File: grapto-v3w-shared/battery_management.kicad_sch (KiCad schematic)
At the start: 18 parts, among them U8 AP9211S-AL, U9 MCP7383x-2xMC

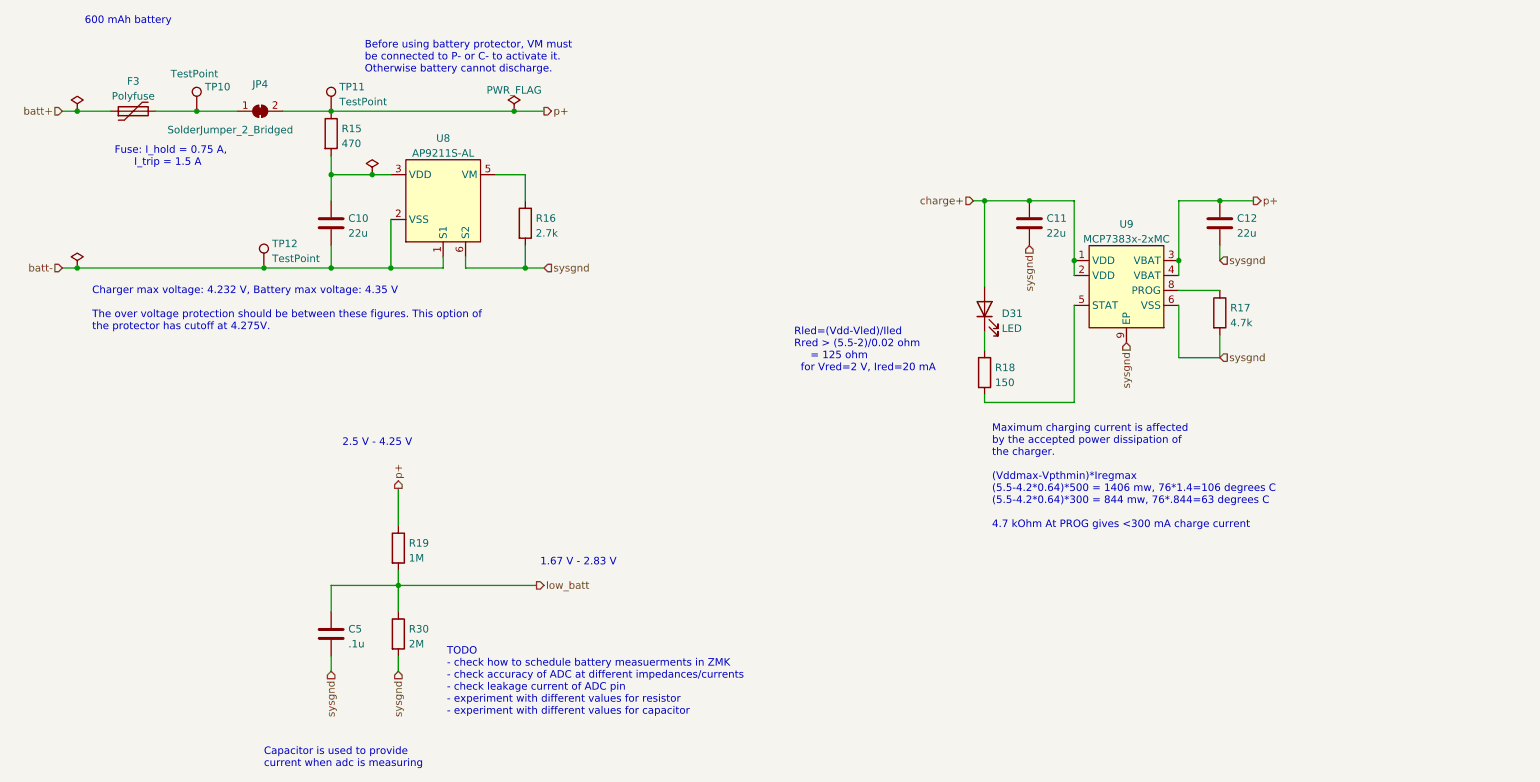
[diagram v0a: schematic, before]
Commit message: Redesign pcb with new mcu and charger
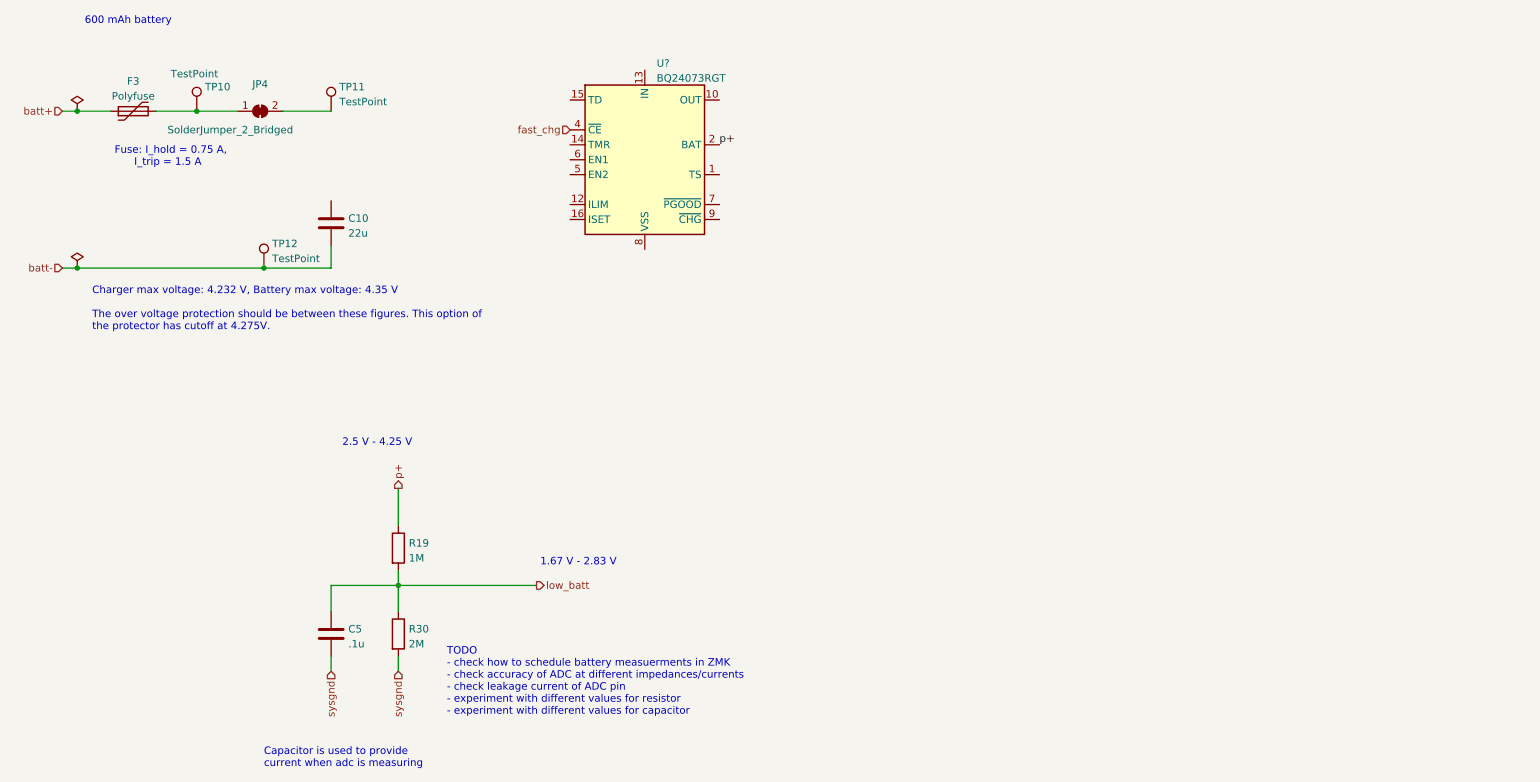
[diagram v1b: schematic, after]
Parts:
- removed C11, C12: 22u, Fuse:Fuse_0603_1608Metric_Pad1.05x0.95mm_HandSolder, symbol Device:C
- removed D31: LED, LED_SMD:LED_0805_2012Metric_Pad1.15x1.40mm_HandSolder, symbol Device:LED
- removed R15: 470, Resistor_SMD:R_0603_1608Metric_Pad0.98x0.95mm_HandSolder, symbol Device:R
- removed R16: 2.7k, Resistor_SMD:R_0603_1608Metric_Pad0.98x0.95mm_HandSolder, symbol Device:R
- removed R17: 4.7k, Resistor_SMD:R_0603_1608Metric_Pad0.98x0.95mm_HandSolder, symbol Device:R
- removed R18: 150, Resistor_SMD:R_0603_1608Metric_Pad0.98x0.95mm_HandSolder, symbol Device:R
- removed U8: AP9211S-AL, grapto-v3w:U-DFN2030-6_type_c, symbol grapto-v3w:AP9211S-AL
- removed U9: MCP7383x-2xMC, Package_DFN_QFN:DFN-8-1EP_3x2mm_P0.5mm_EP1.75x1.45mm, symbol grapto-v3w:MCP7383x-2xMC
- added U?: BQ24073RGT, Package_DFN_QFN:VQFN-16-1EP_3x3mm_P0.5mm_EP1.6x1.6mm, symbol Battery_Management:BQ24073RGT
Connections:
- net p+: now also U?.2 (BAT), U?.3 (BAT); no longer JP4.2 (B), TP11.1
- new net: JP4.2 (B), TP11.1
- new net: U?.10 (OUT), U?.11 (OUT)
- new net: U?.17 (VSS), U?.8 (VSS)
- new net fast_chg: U?.4 (~{CE})
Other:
- note removed: "Before using battery protector, VM must be connected to P- or C- to activate it. Otherwise battery cannot discharge."
- note removed: "Maximum charging current is affected by the accepted power dissipation of the charger. (Vddmax-Vpthmin)*Iregmax (5.5-4.2*0.64)*500 = 1406 mw, 76*1.4=106 degrees C (5.5-4.2*0.64)*300 = 844 mw, 76*.844=63 degrees C 4.7 kOhm At PROG gives <300 mA charge current"
- note removed: "Rled=(Vdd-Vled)/Iled Rred > (5.5-2)/0.02 ohm = 125 ohm for Vred=2 V, Ired=20 mA"

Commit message: schematic rewrite draft done.
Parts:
- removed TP12: TestPoint, grapto-v3w:TestPoint_THTPad_D2.0mm_Drill1.0mm, symbol Connector:TestPoint
- added C1: 1u, Fuse:Fuse_0603_1608Metric_Pad1.05x0.95mm_HandSolder, symbol Device:C
- added D31, D32, D33: LED, LED_SMD:LED_0805_2012Metric_Pad1.15x1.40mm_HandSolder, symbol Device:LED
- added R2, R3, R5: 60, Resistor_SMD:R_0603_1608Metric_Pad0.98x0.95mm_HandSolder, symbol Device:R
- added R4: 10K, Resistor_SMD:R_0603_1608Metric_Pad0.98x0.95mm_HandSolder, symbol Device:R
- added R6: 5.6, Resistor_SMD:R_0603_1608Metric_Pad0.98x0.95mm_HandSolder, symbol Device:R
- added R7: 3.3K, Resistor_SMD:R_0603_1608Metric_Pad0.98x0.95mm_HandSolder, symbol Device:R
- added R8: 2.2K, Resistor_SMD:R_0603_1608Metric_Pad0.98x0.95mm_HandSolder, symbol Device:R
- gave numbers to parts that had none: 1
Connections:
- net batt- is gone; now on net sysgnd: C10.2
- net p+ is gone; now on net bat_fused: R19.1, U2.2 (BAT), U2.3 (BAT)
- net fast_chg: now also U2.5 (EN2), R6.1; no longer U2.4 (~{CE})
- net sysgnd: now also U2.15 (TD), U2.17 (VSS), U2.4 (~{CE}), U2.6 (EN1), U2.8 (VSS), C1.2, D33.1 (K), R4.2, R7.2, R8.2
- net bat_fused: now reaches JP4.2 (B), TP11.1
- net bat_fused: now also C10.1
- net at U2.1 (TS): now also R4.1
- net vsys: now reaches U2.10 (OUT), U2.11 (OUT)
- net vsys: now also R2.1, R3.1
- net at U2.12 (ILIM): now also R7.1
- net vusb: now reaches U2.13 (IN)
- net vusb: now also C1.1
- net at U2.16 (ISET): now also R8.1
- net at U2.7 (~{PGOOD}): now also D32.1 (K)
- net at U2.9 (~{CHG}): now also D31.1 (K)
- net batt+ renamed bat+
- net low_batt renamed bat_level
- new net: R2.2, R5.1
- new net: D32.2 (A), R5.2
- new net: D31.2 (A), R3.2
- new net: D33.2 (A), R6.2
- no-connect marks 0 -> 1
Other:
- note added: "2 V - 2.93 V"
- note added: "3 V - 4.4 V"
- note added: "Blue"
- note added: "Green"
- note added: "IN cap needs to be smaller than 10 uF to prevent too large USB inrush currents"
- note added: "I_led = 20 mA V_led = 3.25 V R_led = (V - V_led)/I_led R_green = (4.4 - 3.2)/0.02 = 60 ohm R_blue = (3.3 - 3.2)/0.02 = 5 ohm R_red = (4.4 - 2)/0.02 = 120 ohm"
- note added: "RILIM = KILIM/ILIM ~ 1525/0.5 = 3.05 kOhm, Use 3.3 kOhm RISET = KISET/ISET ~ 890/0.4 Ohm = 2.225 KOhm, use 2.2 kOhm ITERM leave unconnected for default termination current TD Connect to ground to enable charger termination TMR leave unconnected for default timer values TS Connect with 10 KOhm resistor to ground (enable charging without batt temp sensor) EN1 connect to logic low to use USB current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"
- note added: "Red"
- note removed: "1.67 V - 2.83 V"
- note removed: "2.5 V - 4.25 V"
- note removed: "Charger max voltage: 4.232 V, Battery max voltage: 4.35 V The over voltage protection should be between these figures. This option of the protector has cutoff at 4.275V."
- moved on the sheet: C10, C5, F3, JP4, R19, R30, TP10, TP11, U2

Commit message: Schematic work.
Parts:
- removed D32: LED, LED_SMD:LED_0805_2012Metric_Pad1.15x1.40mm_HandSolder, symbol Device:LED
- removed R2, R5: 60, Resistor_SMD:R_0603_1608Metric_Pad0.98x0.95mm_HandSolder, symbol Device:R
- removed U2: BQ24073RGT, Package_DFN_QFN:VQFN-16-1EP_3x3mm_P0.5mm_EP1.6x1.6mm, symbol Battery_Management:BQ24073RGT
- added SW?: power slider, symbol Switch:SW_Push_SPDT
- added U?: BQ24075RGT, Package_DFN_QFN:VQFN-16-1EP_3x3mm_P0.5mm_EP1.6x1.6mm, symbol Battery_Management:BQ24075RGT
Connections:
- net bat_fused: now also U?.2 (BAT), U?.3 (BAT)
- net fast_chg: now also U?.5 (EN2)
- net sysgnd: now also SW?.3 (C), U?.17 (VSS), U?.4 (~{CE}), U?.6 (EN1), U?.8 (VSS)
- net vsys: now also U?.10 (OUT), U?.11 (OUT)
- net vusb: now also U?.13 (IN)
- net at R4.1: now also U?.1 (TS)
- net at R8.1: now also U?.16 (ISET)
- net at D31.1 (K): now also U?.9 (~{CHG})
- net at R7.1: now also U?.12 (ILIM)
- new net: SW?.2 (B), U?.15 (SYSOFF)
- no-connect marks 1 -> 3
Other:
- note added: "SYSOFF internally pulled up to bat by high resistor. drive low to disconnect battery"
- note added: "TODO add suicide circuit triggered by mcu to save discharge battery more slowly after cutoff"

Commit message: Schematic fine-tuning.
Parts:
- removed JP4: SolderJumper_2_Bridged, Jumper:SolderJumper-2_P1.3mm_Bridged_RoundedPad1.0x1.5mm, symbol Jumper:SolderJumper_2_Bridged
- added R?: 0.01m, symbol Device:R
- added TP?: TestPoint, grapto-v3w:TestPoint_THTPad_D2.0mm_Drill1.0mm, symbol Connector:TestPoint
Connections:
- net bat_fused: now also R?.2
- net sysgnd: now also SW?.1 (A); no longer SW?.3 (C)
- net at U?.7 (~{PGOOD}): now also TP?.1
- net at F3.2, TP10.1: now also R?.1
- no-connect marks 3 -> 2
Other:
- note added: "~CE internally pulled down by 285kOhm resistor"
- moved on the sheet: R4, SW?
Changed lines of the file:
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@@
 (kicad_sch (version 20211123) (generator eeschema)
   (paper "A4")
-  (junction (at 168.91 69.85) (diameter 0) (color 0 0 0 0)
+  (junction (at 168.91 74.93) (diameter 0) (color 0 0 0 0)
   )
   (junction (at 187.325 49.53) (diameter 0) (color 0 0 0 0)
@@
   (junction (at 69.215 118.745) (diameter 0) (color 0 0 0 0)
   )
-  (no_connect (at 150.495 69.85))
+  (no_connect (at 146.05 62.23))
   (no_connect (at 174.625 72.39))
-  (no_connect (at 200.025 82.55))
-  (wire (pts (xy 168.91 74.93) (xy 168.91 69.85))
-    (stroke (width 0) (type default) (color 0 0 0 0))
-  )
   (wire (pts (xy 172.72 105.41) (xy 187.325 105.41))
     (stroke (width 0) (type default) (color 0 0 0 0))
@@
     (stroke (width 0) (type default) (color 0 0 0 0))
   )
+  (wire (pts (xy 168.91 69.85) (xy 168.91 74.93))
+    (stroke (width 0) (type default) (color 0 0 0 0))
+  )
+  (wire (pts (xy 168.91 74.93) (xy 161.925 74.93))
+    (stroke (width 0) (type default) (color 0 0 0 0))
+  )
   (wire (pts (xy 154.305 77.47) (xy 174.625 77.47))
     (stroke (width 0) (type default) (color 0 0 0 0))
@@
     (stroke (width 0) (type default) (color 0 0 0 0))
   )
-  (wire (pts (xy 205.74 73.66) (xy 211.455 73.66))
+  (wire (pts (xy 211.455 73.66) (xy 217.17 73.66))
     (stroke (width 0) (type default) (color 0 0 0 0))
   )
@@
     (stroke (width 0) (type default) (color 0 0 0 0))
   )
-  (wire (pts (xy 205.74 77.47) (xy 205.74 73.66))
+  (wire (pts (xy 211.455 77.47) (xy 211.455 73.66))
     (stroke (width 0) (type default) (color 0 0 0 0))
   )
@@
     (stroke (width 0) (type default) (color 0 0 0 0))
   )
-  (wire (pts (xy 145.415 69.85) (xy 145.415 73.025))
-    (stroke (width 0) (type default) (color 0 0 0 0))
-  )
   (wire (pts (xy 172.72 96.52) (xy 172.72 105.41))
     (stroke (width 0) (type default) (color 0 0 0 0))
@@
     (stroke (width 0) (type default) (color 0 0 0 0))
   )
-  (wire (pts (xy 156.21 69.85) (xy 168.91 69.85))
-    (stroke (width 0) (type default) (color 0 0 0 0))
-  )
   (wire (pts (xy 174.625 74.93) (xy 168.91 74.93))
     (stroke (width 0) (type default) (color 0 0 0 0))
   )
-  (wire (pts (xy 156.21 58.42) (xy 147.955 58.42))
-    (stroke (width 0) (type default) (color 0 0 0 0))
-  )
   (wire (pts (xy 164.465 82.55) (xy 164.465 88.9))
     (stroke (width 0) (type default) (color 0 0 0 0))
@@
     (stroke (width 0) (type default) (color 0 0 0 0))
   )
-  (wire (pts (xy 200.025 77.47) (xy 205.74 77.47))
+  (wire (pts (xy 200.025 77.47) (xy 211.455 77.47))
     (stroke (width 0) (type default) (color 0 0 0 0))
   )
@@
     (stroke (width 0) (type default) (color 0 0 0 0))
   )
-  (wire (pts (xy 147.955 58.42) (xy 147.955 59.69))
-    (stroke (width 0) (type default) (color 0 0 0 0))
-  )
   (wire (pts (xy 178.435 49.53) (xy 187.325 49.53))
     (stroke (width 0) (type default) (color 0 0 0 0))
   )
-  (wire (pts (xy 211.455 81.28) (xy 211.455 84.455))
+  (wire (pts (xy 217.17 81.28) (xy 217.17 84.455))
     (stroke (width 0) (type default) (color 0 0 0 0))
   )
@@
     (stroke (width 0) (type default) (color 0 0 0 0))
   )
-  (wire (pts (xy 156.21 69.85) (xy 156.21 73.025))
-    (stroke (width 0) (type default) (color 0 0 0 0))
-  )
   (wire (pts (xy 62.23 54.61) (xy 64.77 54.61))
     (stroke (width 0) (type default) (color 0 0 0 0))
@@
     (stroke (width 0) (type default) (color 0 0 0 0))
   )
-  (wire (pts (xy 156.21 64.77) (xy 156.21 58.42))
-    (stroke (width 0) (type default) (color 0 0 0 0))
-  )
   (wire (pts (xy 174.625 85.09) (xy 172.72 85.09))
     (stroke (width 0) (type default) (color 0 0 0 0))
@@
   )
   (wire (pts (xy 69.215 118.745) (xy 69.215 123.19))
-    (stroke (width 0) (type default) (color 0 0 0 0))
-  )
-  (wire (pts (xy 156.21 73.025) (xy 145.415 73.025))
     (stroke (width 0) (type default) (color 0 0 0 0))
   )
@@
     (effects (font (size 1.27 1.27)) (justify left bottom))
   )
+  (text "~CE internally pulled down\nby 285kOhm resistor\n" (at 152.4 74.295 180)
+    (effects (font (size 1.27 1.27)) (justify right bottom))
+  )
   (text "IN cap\nneeds to be smaller than\n10 uF to prevent \ntoo large USB inrush currents"
     (at 191.77 45.72 0)
@@
     (effects (font (size 1.27 1.27)) (justify left bottom))
   )
-  (text "Fuse: I_hold = 0.75 A,\n      I_trip = 1.5 A" (at 75.565 64.77 0)
+  (text "Fuse: I_hold = 0.75 A,\n      I_trip = 1.5 A" (at 64.77 63.5 0)
     (effects (font (size 1.27 1.27)) (justify left bottom))
   )
@@
     (effects (font (size 1.27 1.27)) (justify right))
   )
+  (hierarchical_label "sysgnd" (shape input) (at 146.05 67.31 180)
+    (effects (font (size 1.27 1.27)) (justify right))
+  )
   (hierarchical_label "sysgnd" (shape input) (at 57.785 133.35 270)
     (effects (font (size 1.27 1.27)) (justify right))
@@
     (effects (font (size 1.27 1.27)) (justify right))
   )
-  (hierarchical_label "sysgnd" (shape input) (at 211.455 84.455 0)
+  (hierarchical_label "sysgnd" (shape input) (at 217.17 84.455 0)
     (effects (font (size 1.27 1.27)) (justify left))
   )
@@
     (effects (font (size 1.27 1.27)) (justify right))
   )
-  (hierarchical_label "sysgnd" (shape input) (at 168.91 74.93 180)
+  (hierarchical_label "sysgnd" (shape input) (at 161.925 74.93 180)
     (effects (font (size 1.27 1.27)) (justify right))
   )
@@
     (pin "9")
   )
-  (symbol (lib_id "Switch:SW_Push_SPDT") (at 147.955 64.77 270) (unit 1)
-    (in_bom yes) (on_board yes) (fields_autoplaced)
-    (property "Reference" "SW?" (id 0) (at 151.638 63.9353 90)
-      (effects (font (size 1.27 1.27)) (justify left))
-    )
-    (property "Value" "power slider" (id 1) (at 151.638 66.4722 90)
-      (effects (font (size 1.27 1.27)) (justify left))
-    )
-    (property "Footprint" "" (id 2) (at 147.955 64.77 0)
-      (effects (font (size 1.27 1.27)) hide)
-    )
-    (property "Datasheet" "~" (id 3) (at 147.955 64.77 0)
+  (symbol (lib_id "Device:R") (at 95.885 54.61 90) (unit 1)
+    (in_bom yes) (on_board yes) (fields_autoplaced)
+    (property "Reference" "R?" (id 0) (at 95.885 49.8942 90))
+    (property "Value" "0.01m" (id 1) (at 95.885 52.4311 90))
+    (property "Footprint" "" (id 2) (at 95.885 56.388 90)
+      (effects (font (size 1.27 1.27)) hide)
+    )
+    (property "Datasheet" "~" (id 3) (at 95.885 54.61 0)
+      (effects (font (size 1.27 1.27)) hide)
+    )
+    (pin "1")
+    (pin "2")
+  )
+  (symbol (lib_id "Switch:SW_Push_SPDT") (at 151.13 64.77 180) (unit 1)
+    (in_bom yes) (on_board yes) (fields_autoplaced)
+    (property "Reference" "SW?" (id 0) (at 151.13 58.1492 0))
+    (property "Value" "power slider" (id 1) (at 151.13 60.6861 0))
+    (property "Footprint" "" (id 2) (at 151.13 64.77 0)
+      (effects (font (size 1.27 1.27)) hide)
+    )
+    (property "Datasheet" "~" (id 3) (at 151.13 64.77 0)
       (effects (font (size 1.27 1.27)) hide)
     )
@@
     (pin "3")
   )
-  (symbol (lib_id "Device:R") (at 211.455 77.47 0) (unit 1)
-    (in_bom yes) (on_board yes) (fields_autoplaced)
-    (property "Reference" "R4" (id 0) (at 213.233 76.6353 0)
-      (effects (font (size 1.27 1.27)) (justify left))
-    )
-    (property "Value" "10K" (id 1) (at 213.233 79.1722 0)
-      (effects (font (size 1.27 1.27)) (justify left))
-    )
-    (property "Footprint" "Resistor_SMD:R_0603_1608Metric_Pad0.98x0.95mm_HandSolder" (id 2) (at 209.677 77.47 90)
-      (effects (font (size 1.27 1.27)) hide)
-    )
-    (property "Datasheet" "~" (id 3) (at 211.455 77.47 0)
+  (symbol (lib_id "Device:R") (at 217.17 77.47 0) (unit 1)
+    (in_bom yes) (on_board yes) (fields_autoplaced)
+    (property "Reference" "R4" (id 0) (at 218.948 76.6353 0)
+      (effects (font (size 1.27 1.27)) (justify left))
+    )
+    (property "Value" "10K" (id 1) (at 218.948 79.1722 0)
+      (effects (font (size 1.27 1.27)) (justify left))
+    )
+    (property "Footprint" "Resistor_SMD:R_0603_1608Metric_Pad0.98x0.95mm_HandSolder" (id 2) (at 215.392 77.47 90)
+      (effects (font (size 1.27 1.27)) hide)
+    )
+    (property "Datasheet" "~" (id 3) (at 217.17 77.47 0)
       (effects (font (size 1.27 1.27)) hide)
     )
@@
     (pin "2")
   )
-  (symbol (lib_id "Jumper:SolderJumper_2_Bridged") (at 95.885 54.61 0) (unit 1)
-    (in_bom yes) (on_board yes)
-    (property "Reference" "JP4" (id 0) (at 95.885 50.0212 0))
-    (property "Value" "SolderJumper_2_Bridged" (id 1) (at 90.805 57.785 0))
-    (property "Footprint" "Jumper:SolderJumper-2_P1.3mm_Bridged_RoundedPad1.0x1.5mm" (id 2) (at 95.885 54.61 0)
-      (effects (font (size 1.27 1.27)) hide)
-    )
-    (property "Datasheet" "~" (id 3) (at 95.885 54.61 0)
-      (effects (font (size 1.27 1.27)) hide)
-    )
-    (pin "1")
-    (pin "2")
-  )
   (symbol (lib_id "Device:LED") (at 234.95 80.645 90) (unit 1)
     (in_bom yes) (on_board yes) (fields_autoplaced)
@@
     (pin "2")
   )
+  (symbol (lib_id "Connector:TestPoint") (at 200.025 82.55 270) (unit 1)
+    (in_bom yes) (on_board yes) (fields_autoplaced)
+    (property "Reference" "TP?" (id 0) (at 204.724 81.7153 90)
+      (effects (font (size 1.27 1.27)) (justify left))
+    )
+    (property "Value" "TestPoint" (id 1) (at 204.724 84.2522 90)
+      (effects (font (size 1.27 1.27)) (justify left))
+    )
+    (property "Footprint" "grapto-v3w:TestPoint_THTPad_D2.0mm_Drill1.0mm" (id 2) (at 200.025 87.63 0)
+      (effects (font (size 1.27 1.27)) hide)
+    )
+    (property "Datasheet" "~" (id 3) (at 200.025 87.63 0)
+      (effects (font (size 1.27 1.27)) hide)
+    )
+    (pin "1")
+  )
   (symbol (lib_id "Connector:TestPoint") (at 107.95 54.61 0) (unit 1)
